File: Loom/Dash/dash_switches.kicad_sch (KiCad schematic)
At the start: 5 parts

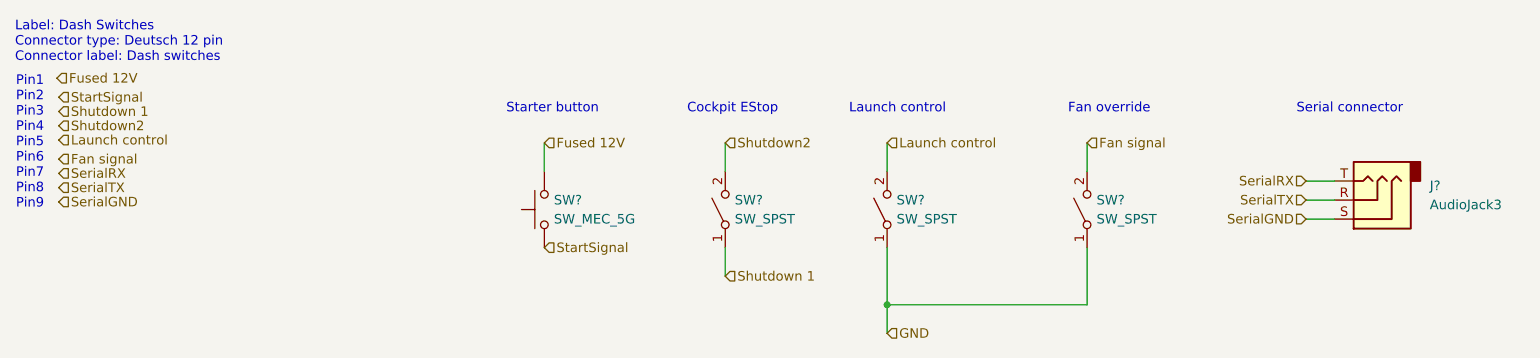
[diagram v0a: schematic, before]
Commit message: Added the neutral and shutdown LEDs to dash
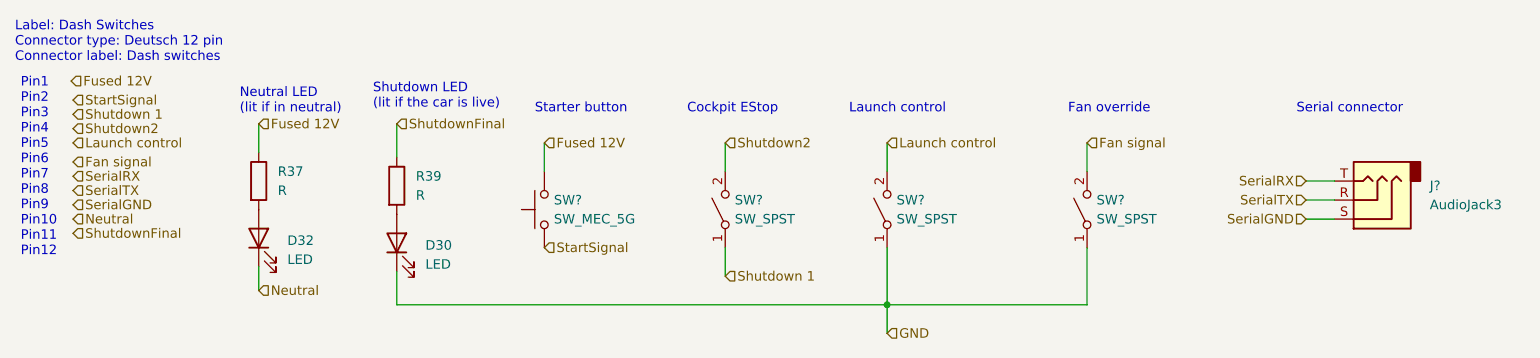
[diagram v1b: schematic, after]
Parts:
- added D30, D32: LED, symbol Device:LED
- added R37, R39: R, symbol Device:R
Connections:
- net Fused 12V: now also R37.1
- net GND: now also D30.1 (K)
- new net: D32.2 (A), R37.2
- new net: D30.2 (A), R39.2
- new net Neutral: D32.1 (K)
- new net ShutdownFinal: R39.1
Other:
- note added: "Neutral LED (lit if in neutral)"
- note added: "Pin1 Pin2 Pin3 Pin4 Pin5 Pin6 Pin7 Pin8 Pin9 Pin10 Pin11 Pin12"
- note added: "Shutdown LED (lit if the car is live)"
- note removed: "Pin1 Pin2 Pin3 Pin4 Pin5 Pin6 Pin7 Pin8 Pin9"
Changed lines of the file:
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@@
+    (stroke (width 0) (type default))
+  )
+  (wire (pts (xy 80.01 74.93) (xy 80.01 78.105))
     (stroke (width 0) (type default))
   )
@@
     (stroke (width 0) (type default))
   )
+  (wire (pts (xy 98.425 75.565) (xy 98.425 80.01))
+    (stroke (width 0) (type default))
+  )
   (wire (pts (xy 142.24 58.42) (xy 142.24 62.23))
     (stroke (width 0) (type default))
@@
     (stroke (width 0) (type default))
   )
+  (wire (pts (xy 98.425 80.01) (xy 163.83 80.01))
+    (stroke (width 0) (type default))
+  )
   (wire (pts (xy 118.11 58.42) (xy 118.11 62.23))
     (stroke (width 0) (type default))
   )
+  (wire (pts (xy 98.425 55.88) (xy 98.425 60.325))
+    (stroke (width 0) (type default))
+  )
+  (wire (pts (xy 80.01 55.88) (xy 80.01 59.69))
+    (stroke (width 0) (type default))
+  )
   (wire (pts (xy 142.24 72.39) (xy 142.24 76.2))
     (stroke (width 0) (type default))
   )
-  (text "Pin1\nPin2\nPin3\nPin4\nPin5\nPin6\nPin7\nPin8\nPin9" (at 47.625 67.31 0)
+  (text "Pin1\nPin2\nPin3\nPin4\nPin5\nPin6\nPin7\nPin8\nPin9\nPin10\nPin11\nPin12"
+    (at 48.26 73.66 0)
     (effects (font (size 1.27 1.27)) (justify left bottom))
   )
@@
     (effects (font (size 1.27 1.27)) (justify left bottom))
   )
-  (text "Starter button" (at 113.03 54.61 0)
+  (text "Shutdown LED\n(lit if the car is live)" (at 95.25 53.975 0)
+    (effects (font (size 1.27 1.27)) (justify left bottom))
+  )
+  (text "Starter button" (at 116.84 54.61 0)
     (effects (font (size 1.27 1.27)) (justify left bottom))
   )
@@
     (effects (font (size 1.27 1.27)) (justify left bottom))
   )
+  (text "Neutral LED\n(lit if in neutral)\n" (at 77.47 54.61 0)
+    (effects (font (size 1.27 1.27)) (justify left bottom))
+  )
+  (hierarchical_label "Neutral" (shape input) (at 80.01 78.105 0) (fields_autoplaced)
+    (effects (font (size 1.27 1.27)) (justify left))
+  )
   (hierarchical_label "SerialRX" (shape input) (at 219.71 63.5 180) (fields_autoplaced)
     (effects (font (size 1.27 1.27)) (justify right))
@@
     (effects (font (size 1.27 1.27)) (justify left))
   )
-  (hierarchical_label "SerialRX" (shape input) (at 53.34 62.484 0) (fields_autoplaced)
-    (effects (font (size 1.27 1.27)) (justify left))
-  )
-  (hierarchical_label "Fused 12V" (shape input) (at 53.086 49.784 0) (fields_autoplaced)
+  (hierarchical_label "SerialRX" (shape input) (at 55.245 62.865 0) (fields_autoplaced)
+    (effects (font (size 1.27 1.27)) (justify left))
+  )
+  (hierarchical_label "Fused 12V" (shape input) (at 54.991 50.165 0) (fields_autoplaced)
     (effects (font (size 1.27 1.27)) (justify left))
   )
@@
     (effects (font (size 1.27 1.27)) (justify left))
   )
-  (hierarchical_label "Shutdown2" (shape input) (at 53.34 56.134 0) (fields_autoplaced)
-    (effects (font (size 1.27 1.27)) (justify left))
-  )
-  (hierarchical_label "Launch control" (shape input) (at 53.34 58.039 0) (fields_autoplaced)
-    (effects (font (size 1.27 1.27)) (justify left))
-  )
-  (hierarchical_label "SerialTX" (shape input) (at 53.34 64.389 0) (fields_autoplaced)
+  (hierarchical_label "Shutdown2" (shape input) (at 55.245 56.515 0) (fields_autoplaced)
+    (effects (font (size 1.27 1.27)) (justify left))
+  )
+  (hierarchical_label "Launch control" (shape input) (at 55.245 58.42 0) (fields_autoplaced)
+    (effects (font (size 1.27 1.27)) (justify left))
+  )
+  (hierarchical_label "Neutral" (shape input) (at 55.245 68.58 0) (fields_autoplaced)
+    (effects (font (size 1.27 1.27)) (justify left))
+  )
+  (hierarchical_label "ShutdownFinal" (shape input) (at 98.425 55.88 0) (fields_autoplaced)
+    (effects (font (size 1.27 1.27)) (justify left))
+  )
+  (hierarchical_label "SerialTX" (shape input) (at 55.245 64.77 0) (fields_autoplaced)
     (effects (font (size 1.27 1.27)) (justify left))
   )
   (hierarchical_label "Shutdown2" (shape input) (at 142.24 58.42 0) (fields_autoplaced)
+    (effects (font (size 1.27 1.27)) (justify left))
+  )
+  (hierarchical_label "ShutdownFinal" (shape input) (at 55.245 70.485 0) (fields_autoplaced)
     (effects (font (size 1.27 1.27)) (justify left))
   )
@@
     (effects (font (size 1.27 1.27)) (justify right))
   )
-  (hierarchical_label "Fan signal" (shape input) (at 53.34 60.579 0) (fields_autoplaced)
+  (hierarchical_label "Fan signal" (shape input) (at 55.245 60.96 0) (fields_autoplaced)
     (effects (font (size 1.27 1.27)) (justify left))
   )
@@
     (effects (font (size 1.27 1.27)) (justify right))
   )
-  (hierarchical_label "SerialGND" (shape input) (at 53.34 66.294 0) (fields_autoplaced)
+  (hierarchical_label "SerialGND" (shape input) (at 55.245 66.675 0) (fields_autoplaced)
+    (effects (font (size 1.27 1.27)) (justify left))
+  )
+  (hierarchical_label "Fused 12V" (shape input) (at 80.01 55.88 0) (fields_autoplaced)
     (effects (font (size 1.27 1.27)) (justify left))
   )
@@
     (effects (font (size 1.27 1.27)) (justify left))
   )
-  (hierarchical_label "StartSignal" (shape input) (at 53.34 52.324 0) (fields_autoplaced)
+  (hierarchical_label "StartSignal" (shape input) (at 55.245 52.705 0) (fields_autoplaced)
     (effects (font (size 1.27 1.27)) (justify left))
   )
@@
     (effects (font (size 1.27 1.27)) (justify left))
   )
-  (hierarchical_label "Shutdown 1" (shape input) (at 53.34 54.229 0) (fields_autoplaced)
-    (effects (font (size 1.27 1.27)) (justify left))
+  (hierarchical_label "Shutdown 1" (shape input) (at 55.245 54.61 0) (fields_autoplaced)
+    (effects (font (size 1.27 1.27)) (justify left))
+  )
+  (symbol (lib_id "Device:LED") (at 80.01 71.12 90) (unit 1)
+    (in_bom yes) (on_board yes) (dnp no) (fields_autoplaced)
+    (property "Reference" "D32" (at 83.82 71.4375 90)
+      (effects (font (size 1.27 1.27)) (justify right))
+    )
+    (property "Value" "LED" (at 83.82 73.9775 90)
+      (effects (font (size 1.27 1.27)) (justify right))
+    )
+    (property "Footprint" "" (at 80.01 71.12 0)
+      (effects (font (size 1.27 1.27)) hide)
+    )
+    (property "Datasheet" "~" (at 80.01 71.12 0)
+      (effects (font (size 1.27 1.27)) hide)
+    )
+    (pin "1")
+    (pin "2")
+    (instances
+      (project "Loom23_detailed"
+        (path "/691c98c8-9b47-40a5-87b6-2865e3f6892d/7b0f0b05-0256-463a-ae57-e387aefb1021"
+          (reference "D32") (unit 1)
+        )
+        (path "/691c98c8-9b47-40a5-87b6-2865e3f6892d/31af8776-e20e-4678-af96-7d5469953b0e"
+          (reference "D31") (unit 1)
+        )
+      )
+    )
+  )
+  (symbol (lib_id "Device:R") (at 80.01 63.5 0) (unit 1)
+    (in_bom yes) (on_board yes) (dnp no) (fields_autoplaced)
+    (property "Reference" "R37" (at 82.55 62.23 0)
+      (effects (font (size 1.27 1.27)) (justify left))
+    )
+    (property "Value" "R" (at 82.55 64.77 0)
+      (effects (font (size 1.27 1.27)) (justify left))
+    )
+    (property "Footprint" "" (at 78.232 63.5 90)
+      (effects (font (size 1.27 1.27)) hide)
+    )
+    (property "Datasheet" "~" (at 80.01 63.5 0)
+      (effects (font (size 1.27 1.27)) hide)
+    )
+    (pin "1")
+    (pin "2")
+    (instances
+      (project "Loom23_detailed"
+        (path "/691c98c8-9b47-40a5-87b6-2865e3f6892d/7b0f0b05-0256-463a-ae57-e387aefb1021"
+          (reference "R37") (unit 1)
+        )
+        (path "/691c98c8-9b47-40a5-87b6-2865e3f6892d/31af8776-e20e-4678-af96-7d5469953b0e"
+          (reference "R36") (unit 1)
+        )
+      )
+    )
   )
   (symbol (lib_id "Switch:SW_SPST") (at 142.24 67.31 90) (unit 1)
@@
         (path "/691c98c8-9b47-40a5-87b6-2865e3f6892d/31af8776-e20e-4678-af96-7d5469953b0e"
           (reference "SW?") (unit 1)
+        )
+      )
+    )
+  )
+  (symbol (lib_id "Device:LED") (at 98.425 71.755 90) (unit 1)
+    (in_bom yes) (on_board yes) (dnp no) (fields_autoplaced)
+    (property "Reference" "D30" (at 102.235 72.0725 90)
+      (effects (font (size 1.27 1.27)) (justify right))
+    )
+    (property "Value" "LED" (at 102.235 74.6125 90)
+      (effects (font (size 1.27 1.27)) (justify right))
+    )
+    (property "Footprint" "" (at 98.425 71.755 0)
+      (effects (font (size 1.27 1.27)) hide)
+    )
+    (property "Datasheet" "~" (at 98.425 71.755 0)
+      (effects (font (size 1.27 1.27)) hide)
+    )
+    (pin "1")
+    (pin "2")
+    (instances
+      (project "Loom23_detailed"
+        (path "/691c98c8-9b47-40a5-87b6-2865e3f6892d/7b0f0b05-0256-463a-ae57-e387aefb1021"
+          (reference "D30") (unit 1)
+        )
+        (path "/691c98c8-9b47-40a5-87b6-2865e3f6892d/31af8776-e20e-4678-af96-7d5469953b0e"
+          (reference "D29") (unit 1)
         )
       )
@@
         )
       )
+    )
+  )
+  (symbol (lib_id "Device:R") (at 98.425 64.135 0) (unit 1)
+    (in_bom yes) (on_board yes) (dnp no) (fields_autoplaced)
+    (property "Reference" "R39" (at 100.965 62.865 0)
+      (effects (font (size 1.27 1.27)) (justify left))
+    )
+    (property "Value" "R" (at 100.965 65.405 0)
+      (effects (font (size 1.27 1.27)) (justify left))
+    )
+    (property "Footprint" "" (at 96.647 64.135 90)
+      (effects (font (size 1.27 1.27)) hide)
+    )
+    (property "Datasheet" "~" (at 98.425 64.135 0)
+      (effects (font (size 1.27 1.27)) hide)
+    )
+    (pin "1")
+    (pin "2")
+    (instances
+      (project "Loom23_detailed"
+        (path "/691c98c8-9b47-40a5-87b6-2865e3f6892d/7b0f0b05-0256-463a-ae57-e387aefb1021"
+          (reference "R39") (unit 1)
+        )
+        (path "/691c98c8-9b47-40a5-87b6-2865e3f6892d/31af8776-e20e-4678-af96-7d5469953b0e"
+          (reference "R38") (unit 1)
+        )
+      )
